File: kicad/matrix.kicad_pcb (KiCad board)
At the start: 2 copper layers, 110.7 x 76.2 mm, 20 parts, among them J1 Conn_01x08, U1 TLC59025, U10 P-FET, U11 P-FET, U2 74HC595, U3 74HC595, U4 P-FET, U5 P-FET, U6 P-FET, U7 P-FET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

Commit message: Finished most of the layout
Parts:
- moved U4 22.9 mm to (147.3, 44.8)
- moved U7 22.9 mm to (124.5, 44.8)
- moved C3 16.6 mm to (147.1, 67.3), turned to 0 degrees
- moved U5 7.62 mm to (139.7, 44.8)
- moved U6 7.62 mm to (132.1, 44.8)
- moved C1 4.35 mm to (134.9, 68.1), turned to 90 degrees
- turned U2 to 270 degrees
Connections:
- J1 pad 1: /ROWCLK -> /LE
- J1 pad 2: /ROWSDI -> /COLCLK
- J1 pad 3: /~OE -> /COLSDI
- J1 pad 4: /LE -> /~OE
- J1 pad 5: /COLCLK -> /ROWSDI
- J1 pad 6: /COLSDI -> /ROWCLK
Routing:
- net /ROW8: track 0.00 -> 115.8 mm, vias 0 -> 3
- net /ROW6: track 0.00 -> 113.6 mm, vias 0 -> 5
- net /ROW3: track 0.00 -> 112.9 mm, vias 0 -> 1
- net /ROW7: track 0.00 -> 106.9 mm, vias 0 -> 3
- net /ROW5: track 0.00 -> 99.1 mm, vias 0 -> 3
- net /ROW11: track 0.00 -> 95.0 mm
- net /ROW14: track 0.00 -> 84.6 mm, vias 0 -> 3
- net /ROW4: track 0.00 -> 80.4 mm, vias 0 -> 1
- net /ROW1: track 0.00 -> 78.1 mm, vias 0 -> 1
- net /ROW13: track 0.00 -> 77.2 mm, vias 0 -> 2
- net /ROW16: track 0.00 -> 74.7 mm, vias 0 -> 2
- net /ROW15: track 0.00 -> 69.0 mm, vias 0 -> 3
- net /ROW2: track 0.00 -> 67.9 mm, vias 0 -> 1
- net /~OE: track 0.00 -> 59.3 mm, vias 0 -> 4
- net /LE: track 0.00 -> 58.1 mm, vias 0 -> 2
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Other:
- board text added: "GND VCC RCLK RSDI ~OE CSDI CCLK LE"
- board text removed: "GND VCC CSDI CCLK LE ~OE RSDI RCLK"

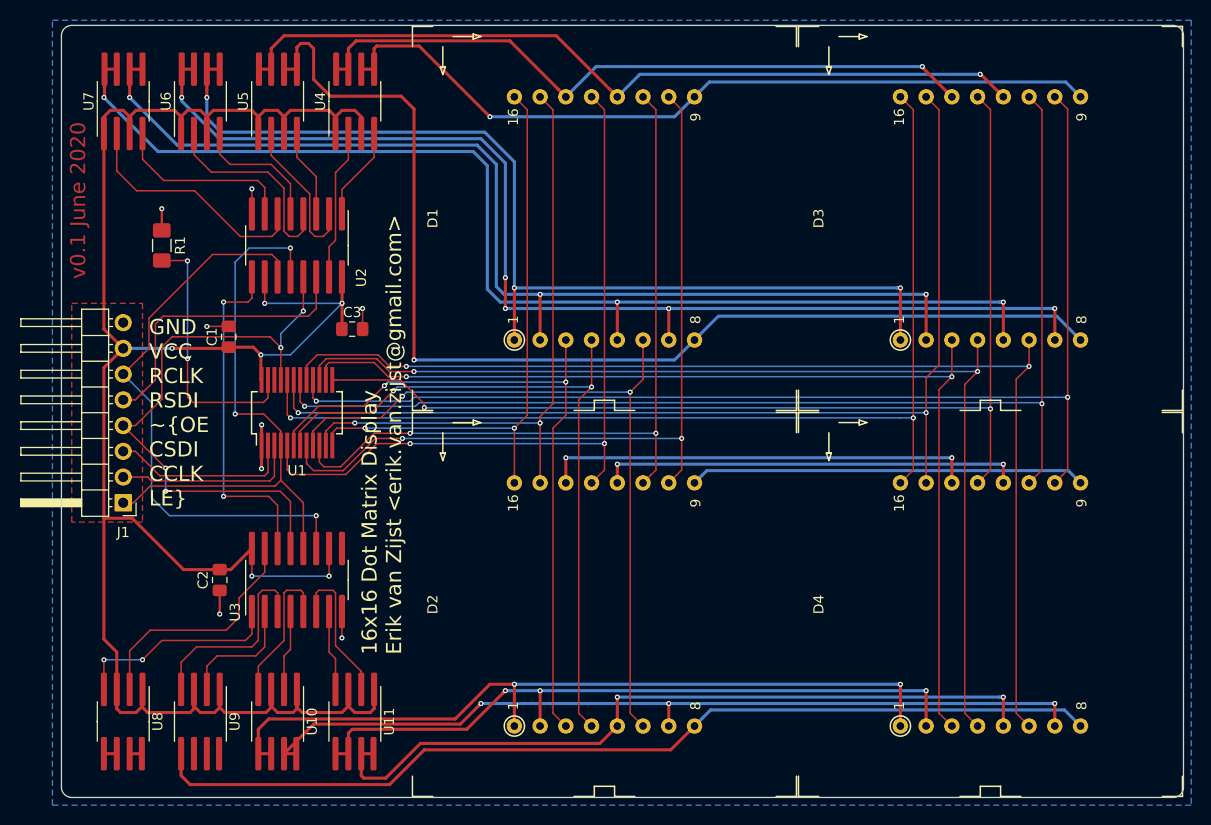
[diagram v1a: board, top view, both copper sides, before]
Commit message: Scaled up 3d display models
Also wired up the remaining nets.
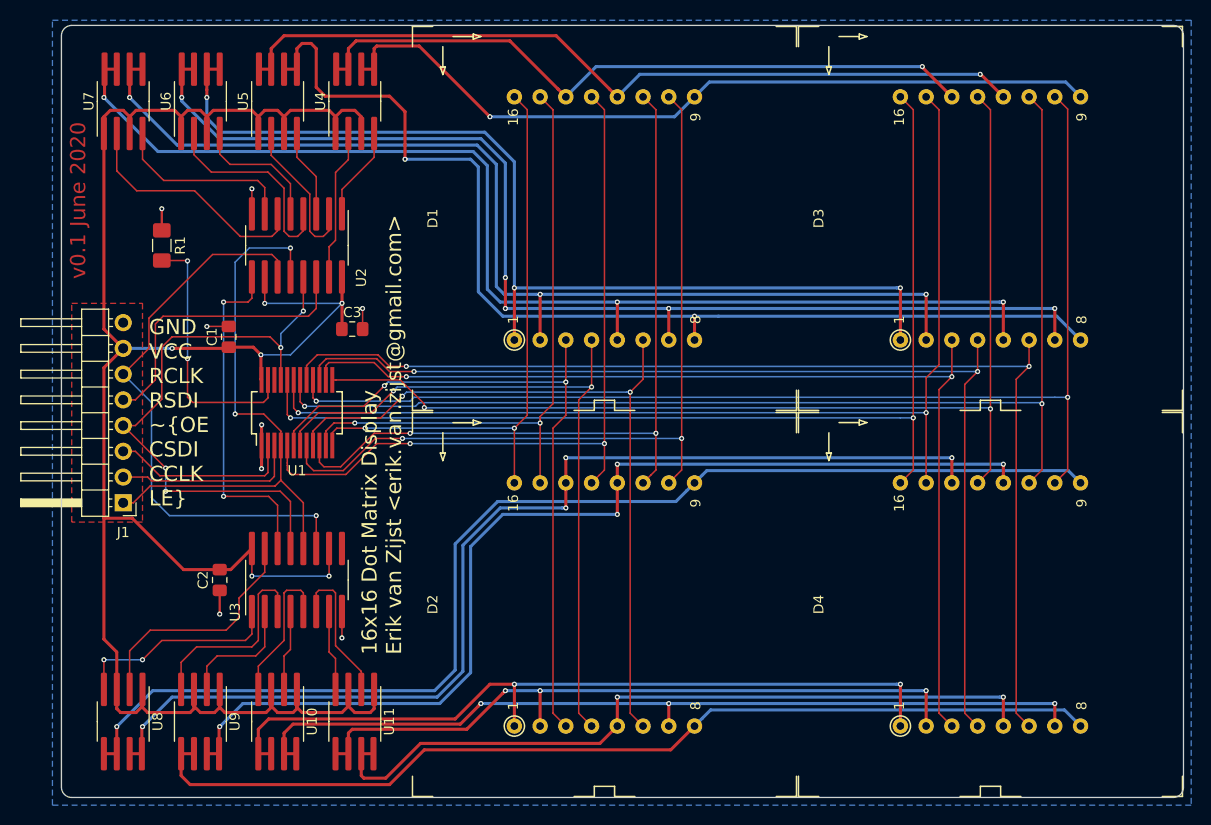
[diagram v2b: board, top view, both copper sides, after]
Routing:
- net /ROW9: track 40.4 -> 117.3 mm, vias 0 -> 1
- net /ROW10: track 44.3 -> 107.4 mm, vias 2 -> 4
- net /ROW12: track 41.8 -> 104.0 mm, vias 2 -> 4
- net /ROW3: track 112.9 -> 107.5 mm, vias 1 -> 2
- net /ROW11: track 95.0 -> 96.3 mm
- net /ROW14: track 84.6 -> 85.8 mm
